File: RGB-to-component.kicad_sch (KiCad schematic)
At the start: 59 parts, among them U2 THS7374

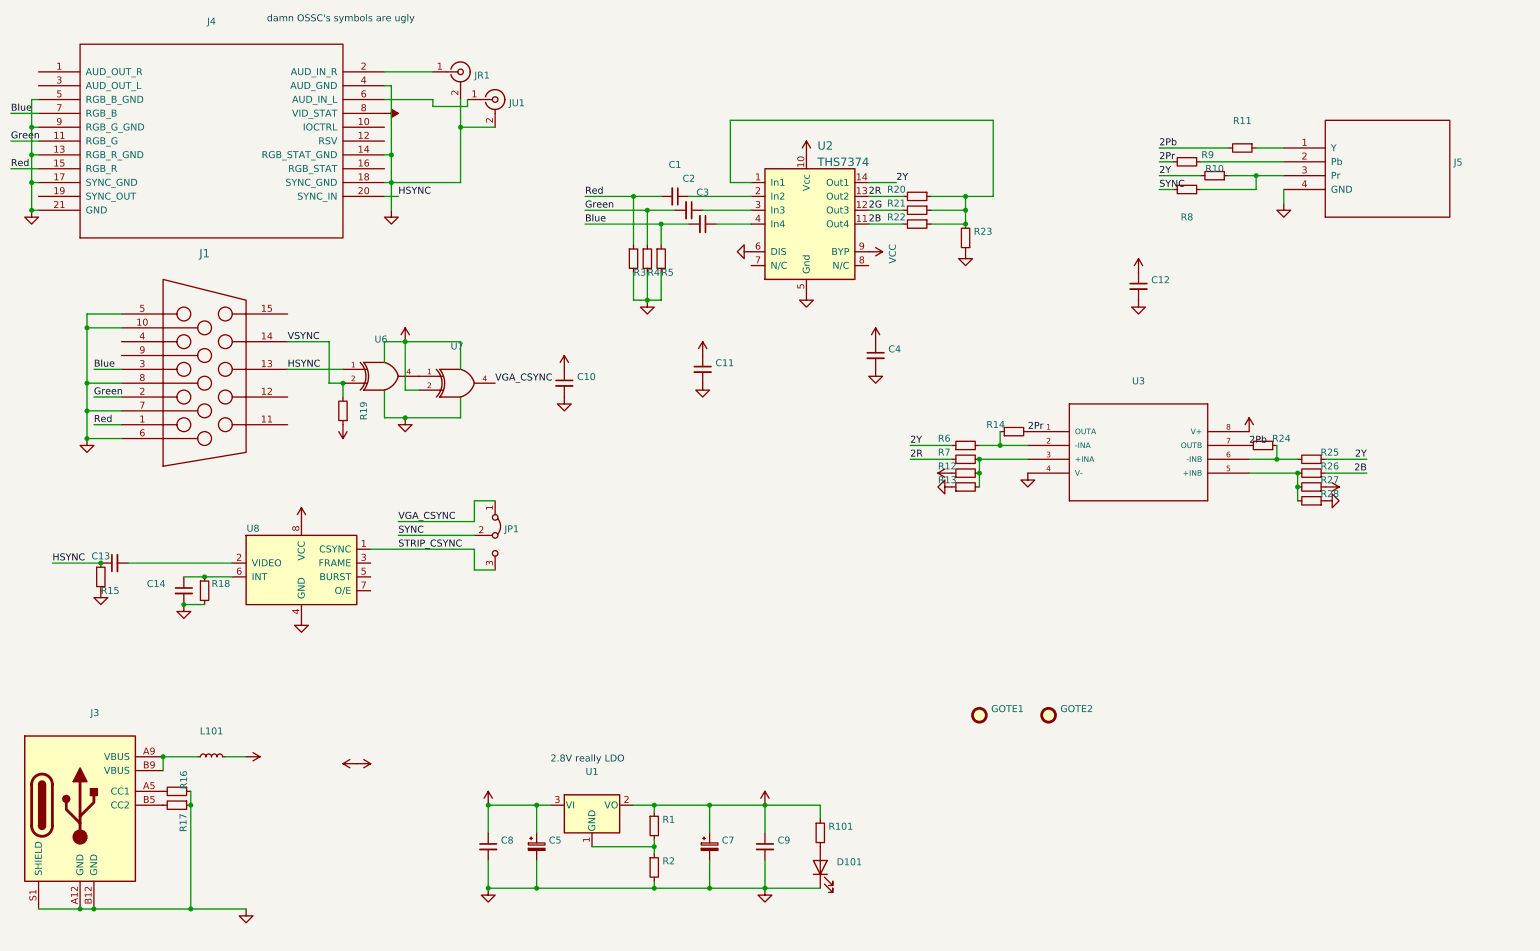
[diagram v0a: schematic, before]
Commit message: return to THS7374 (temporary single board only)
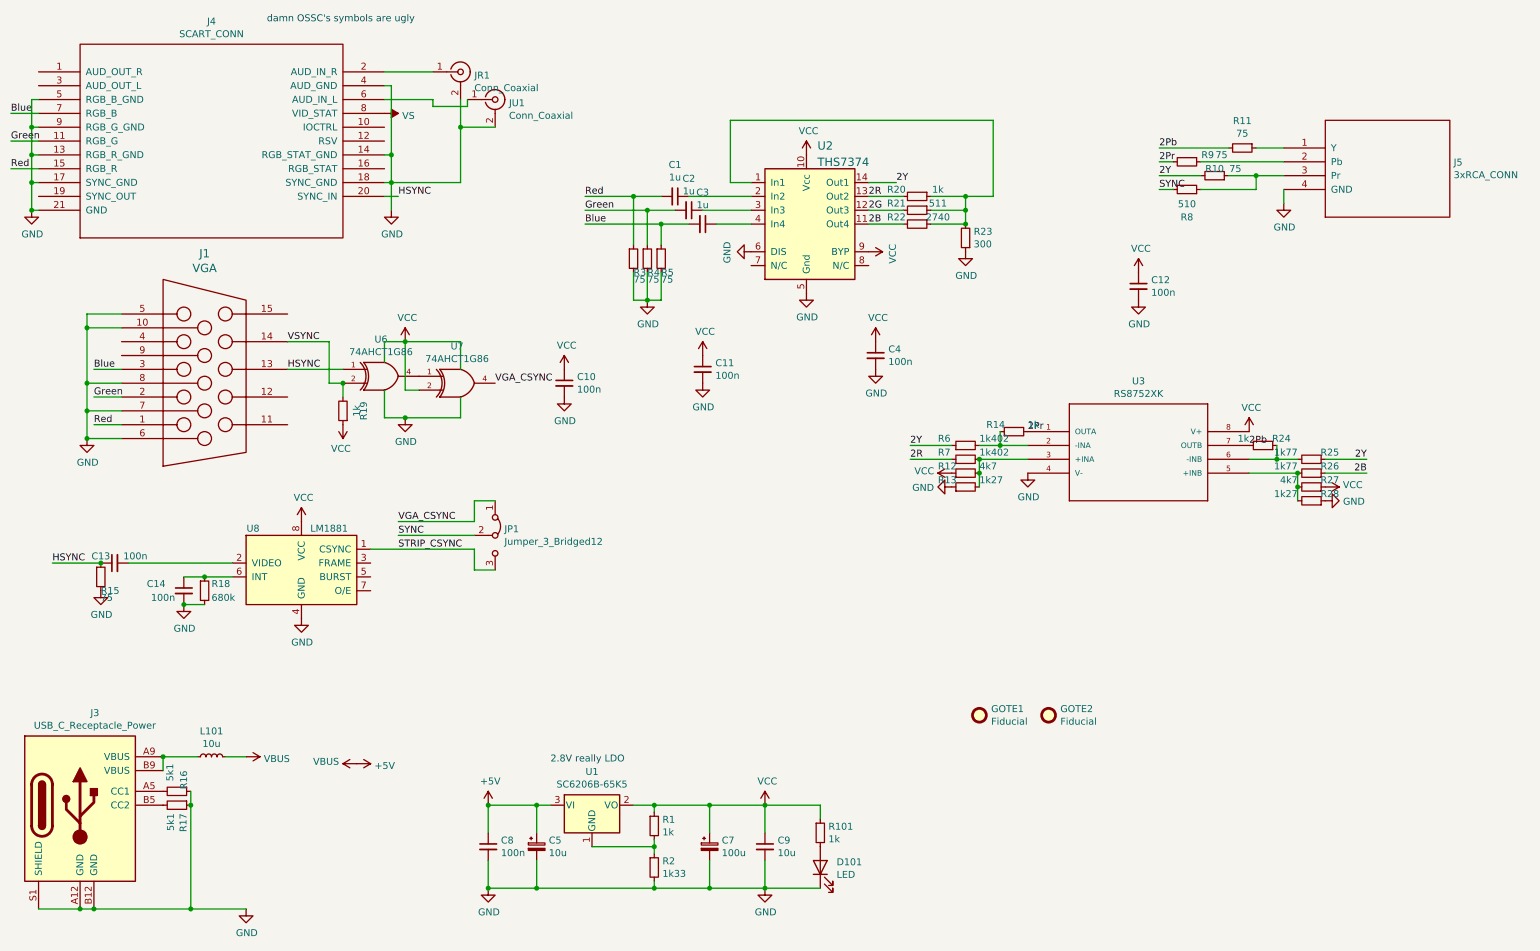
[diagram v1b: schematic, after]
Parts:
- C1, C2, C3: value (none) -> 1u; footprint (none) -> Capacitor_SMD:C_0805_2012Metric_Pad1.15x1.40mm_HandSolder
- C10, C11, C12, C13, C14, C4, C8: value (none) -> 100n; footprint (none) -> Capacitor_SMD:C_0805_2012Metric_Pad1.15x1.40mm_HandSolder
- C5: value (none) -> 10u; footprint (none) -> Capacitor_Tantalum_SMD:CP_EIA-3216-18_Kemet-A_Pad1.58x1.35mm_HandSolder
- C7: value (none) -> 100u; footprint (none) -> Capacitor_Tantalum_SMD:CP_EIA-3528-21_Kemet-B_Pad1.50x2.35mm_HandSolder
- C9: value (none) -> 10u; footprint (none) -> Capacitor_SMD:C_0805_2012Metric_Pad1.15x1.40mm_HandSolder
- D101: value (none) -> LED; footprint (none) -> LED_SMD:LED_0805_2012Metric
- GOTE1: value (none) -> Fiducial; footprint (none) -> videobits:uwuriel
- GOTE2: value (none) -> Fiducial; footprint (none) -> videobits:borgar
- J1: value (none) -> VGA; footprint (none) -> custom_components:VGA_CONN
- J3: value (none) -> USB_C_Receptacle_Power; footprint (none) -> videobits:USB_C_Receptacle_Generic_Power_Only
- J4: value (none) -> SCART_CONN; footprint (none) -> custom_components:SCART_CONN
- J5: value (none) -> 3xRCA_CONN; footprint (none) -> videobits:3xRCA_CONN_SINGLE
- JP1: value (none) -> Jumper_3_Bridged12; footprint (none) -> Jumper:SolderJumper-3_P1.3mm_Bridged12_Pad1.0x1.5mm
- JR1, JU1: value (none) -> Conn_Coaxial; footprint (none) -> videobits:Cheapo_RCA_single_edge
- L101: value (none) -> 10u; footprint (none) -> Inductor_SMD:L_0805_2012Metric_Pad1.15x1.40mm_HandSolder
- R1, R101, R14, R19, R20, R24: value (none) -> 1k; footprint (none) -> Resistor_SMD:R_0805_2012Metric_Pad1.15x1.40mm_HandSolder
- R10, R11, R15, R3, R4, R5, R9: value (none) -> 75; footprint (none) -> Resistor_SMD:R_0805_2012Metric_Pad1.15x1.40mm_HandSolder
- R12, R27: value (none) -> 4k7; footprint (none) -> Resistor_SMD:R_0805_2012Metric_Pad1.15x1.40mm_HandSolder
- R13, R28: value (none) -> 1k27; footprint (none) -> Resistor_SMD:R_0805_2012Metric_Pad1.15x1.40mm_HandSolder
- R16, R17: value (none) -> 5k1; footprint (none) -> Resistor_SMD:R_0805_2012Metric_Pad1.15x1.40mm_HandSolder
- R18: value (none) -> 680k; footprint (none) -> Resistor_SMD:R_0805_2012Metric_Pad1.15x1.40mm_HandSolder
- R2: value (none) -> 1k33; footprint (none) -> Resistor_SMD:R_0805_2012Metric_Pad1.15x1.40mm_HandSolder
- R21: value (none) -> 511; footprint (none) -> Resistor_SMD:R_0805_2012Metric_Pad1.15x1.40mm_HandSolder
- R22: value (none) -> 2740; footprint (none) -> Resistor_SMD:R_0805_2012Metric_Pad1.15x1.40mm_HandSolder
- R23: value (none) -> 300; footprint (none) -> Resistor_SMD:R_0805_2012Metric_Pad1.15x1.40mm_HandSolder
- R25, R26: value (none) -> 1k77; footprint (none) -> Resistor_SMD:R_0805_2012Metric_Pad1.15x1.40mm_HandSolder
- R6, R7: value (none) -> 1k402; footprint (none) -> Resistor_SMD:R_0805_2012Metric_Pad1.15x1.40mm_HandSolder
- R8: value (none) -> 510; footprint (none) -> Resistor_SMD:R_0805_2012Metric_Pad1.15x1.40mm_HandSolder
- U1: value (none) -> SC6206B-65K5; footprint (none) -> Package_TO_SOT_SMD:SOT-23
- U2: footprint (none) -> Package_SO:TSSOP-14_4.4x5mm_P0.65mm
- U3: value (none) -> RS8752XK; footprint (none) -> Package_SO:SOIC-8_3.9x4.9mm_P1.27mm
- U6, U7: value (none) -> 74AHCT1G86; footprint (none) -> Package_TO_SOT_SMD:SOT-23-5
- U8: value (none) -> LM1881; footprint (none) -> Package_SO:SOIC-8_3.9x4.9mm_P1.27mm

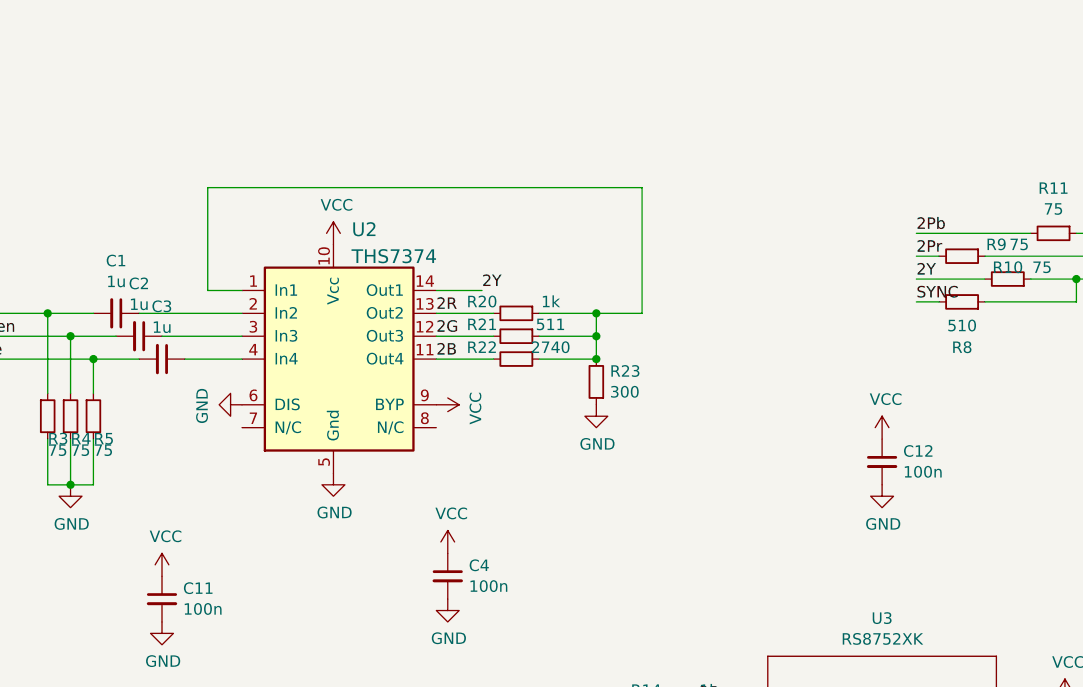
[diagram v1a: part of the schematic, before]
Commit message: swapping video amps again to TPF141 for JLC availability
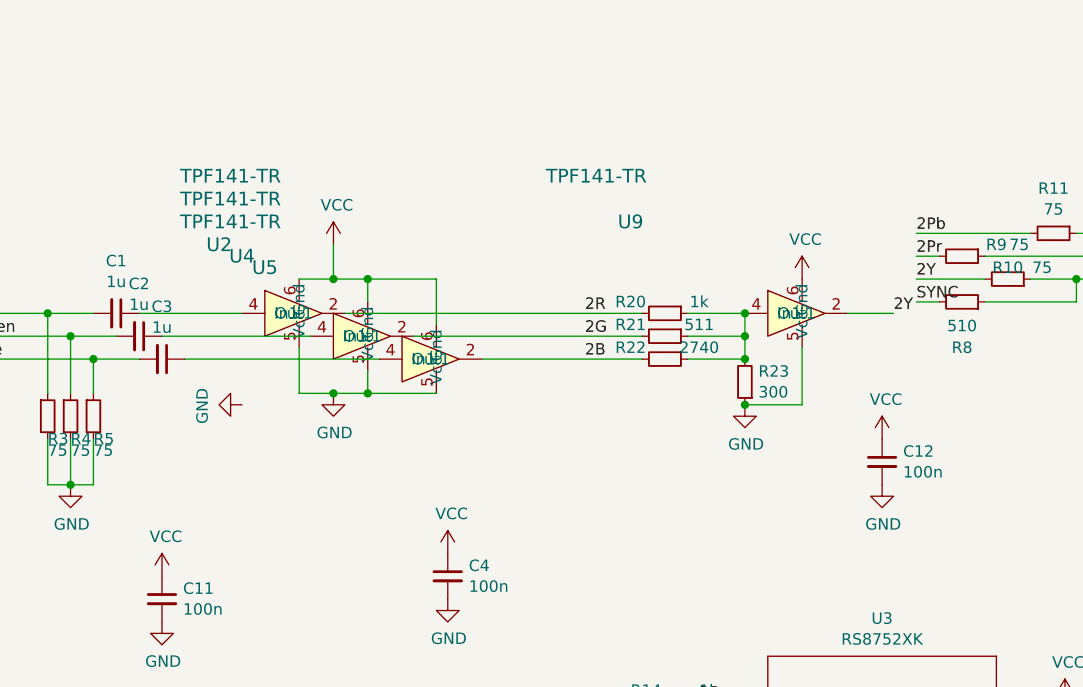
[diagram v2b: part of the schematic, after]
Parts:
- removed U2: THS7374, Package_SO:TSSOP-14_4.4x5mm_P0.65mm, symbol videobits:THS7374
- added U2, U4, U5, U9: TPF141-TR, Package_TO_SOT_SMD:SOT-23-6_Handsoldering, symbol videobits:TPF141-TR
- U1: LCSC C88294 -> C130827
- U8: LCSC C357809 -> C518922
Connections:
- net 2B: now also U5.2 (Out1)
- net 2G: now also U4.2 (Out1)
- net 2R: now also U2.2 (Out1)
- net 2Y: now also U9.2 (Out1)
- net GND: now also U2.5 (Gnd), U4.5 (Gnd), U5.5 (Gnd), U9.5 (Gnd)
- net VCC: now also U2.6 (Vcc), U4.6 (Vcc), U5.6 (Vcc), U9.6 (Vcc)
- net at C1.1: now also U2.4 (In1)
- net at C2.1: now also U4.4 (In1)
- net at C3.1: now also U5.4 (In1)
- net at R20.1, R21.1, R22.1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: now also U9.4 (In1)
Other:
- moved on the sheet: R20, R21, R22, R23

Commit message: updated to kicad 7
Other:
- title: VGA/SHART to YPbPr converter -> VGA/SCART to YPbPr converter

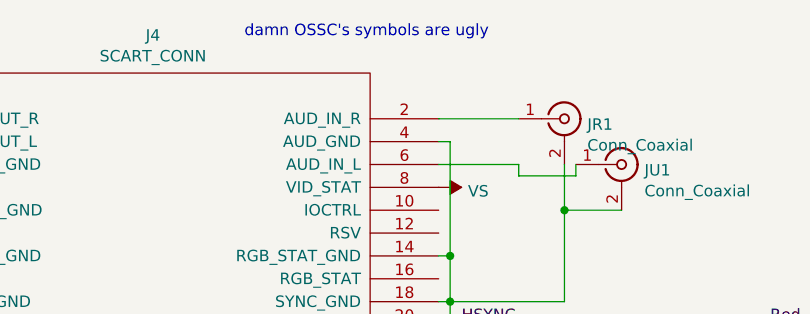
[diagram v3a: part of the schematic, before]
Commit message: kicad update, oscillator footprint replaced
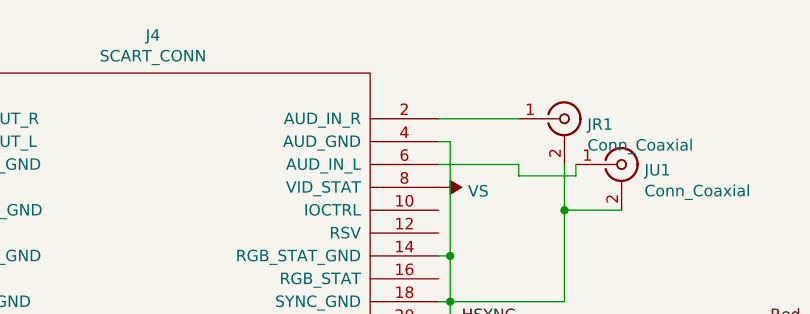
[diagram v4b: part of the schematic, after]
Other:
- note removed: "damn OSSC's symbols are ugly"
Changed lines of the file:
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@@
-    (effects (font (size 1.27 1.27)) (justify left bottom))
-  )
-  (text "damn OSSC's symbols are ugly" (at 62.23 16.51 0)
     (effects (font (size 1.27 1.27)) (justify left bottom))
   )

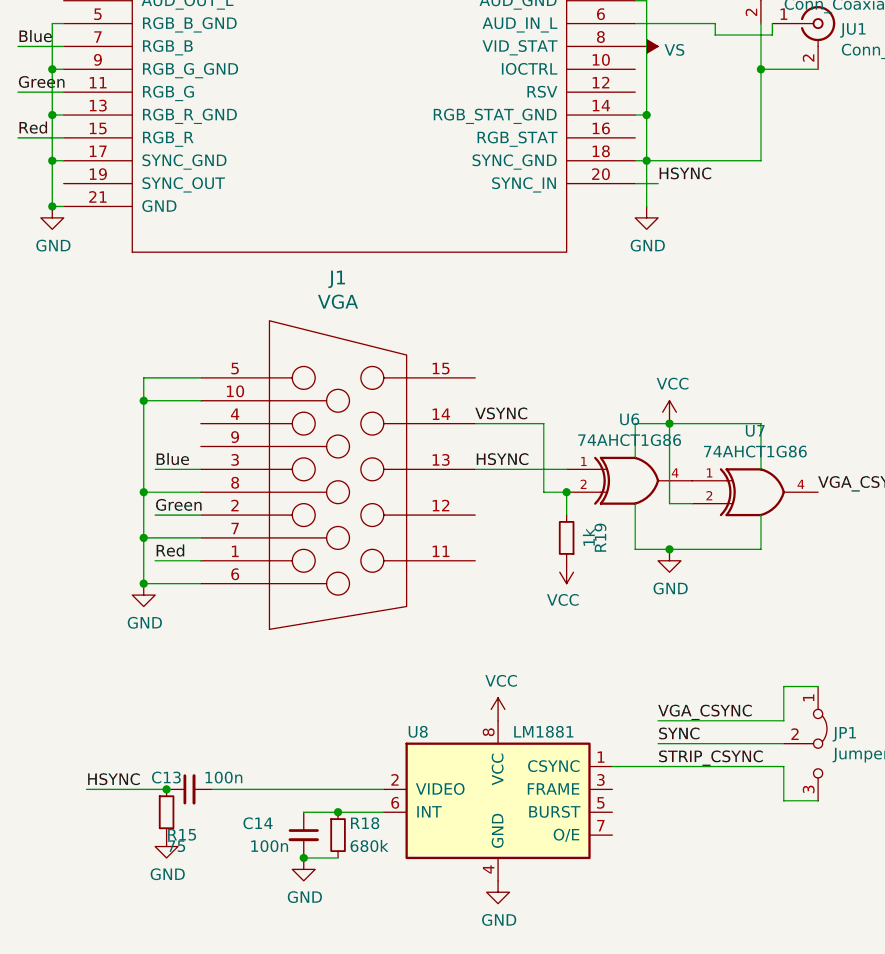
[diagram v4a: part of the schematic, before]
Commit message: 75 ohm removed from hsync, only terminates scart's csync
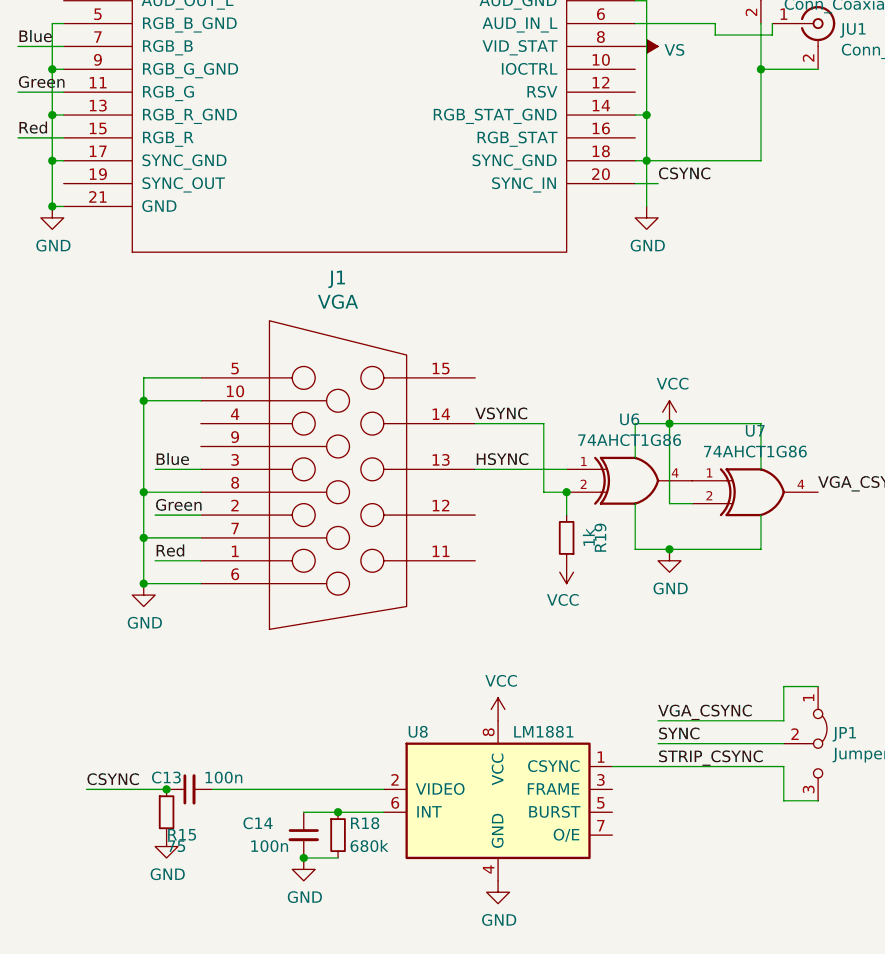
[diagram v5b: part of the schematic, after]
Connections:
- net HSYNC: no longer C13.1, J4.20 (SYNC_IN), R15.1
- new net CSYNC: C13.1, J4.20 (SYNC_IN), R15.1
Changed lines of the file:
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@@
     (effects (font (size 1.27 1.27)) (justify left bottom))
   )
-  (label "HSYNC" (at 86.36 48.26 0) (fields_autoplaced)
+  (label "CSYNC" (at 86.36 48.26 0) (fields_autoplaced)
     (effects (font (size 1.27 1.27)) (justify left bottom))
   )
@@
     (effects (font (size 1.27 1.27)) (justify left bottom))
   )
-  (label "HSYNC" (at 22.86 115.57 0) (fields_autoplaced)
+  (label "CSYNC" (at 22.86 115.57 0) (fields_autoplaced)
     (effects (font (size 1.27 1.27)) (justify left bottom))
   )
